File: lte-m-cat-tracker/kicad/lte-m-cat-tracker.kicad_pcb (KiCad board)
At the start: 2 copper layers, 30 x 35 mm, 32 parts, among them J1 JST-GH-1.25mm-2P, J2 USB-C-16P, SW1 MSK12C02, U1 SIM7080G-M, U2 ESP32-C3, U3 LIS2DW12TR, U4 TP4056, U5 XC6220B331MR-G

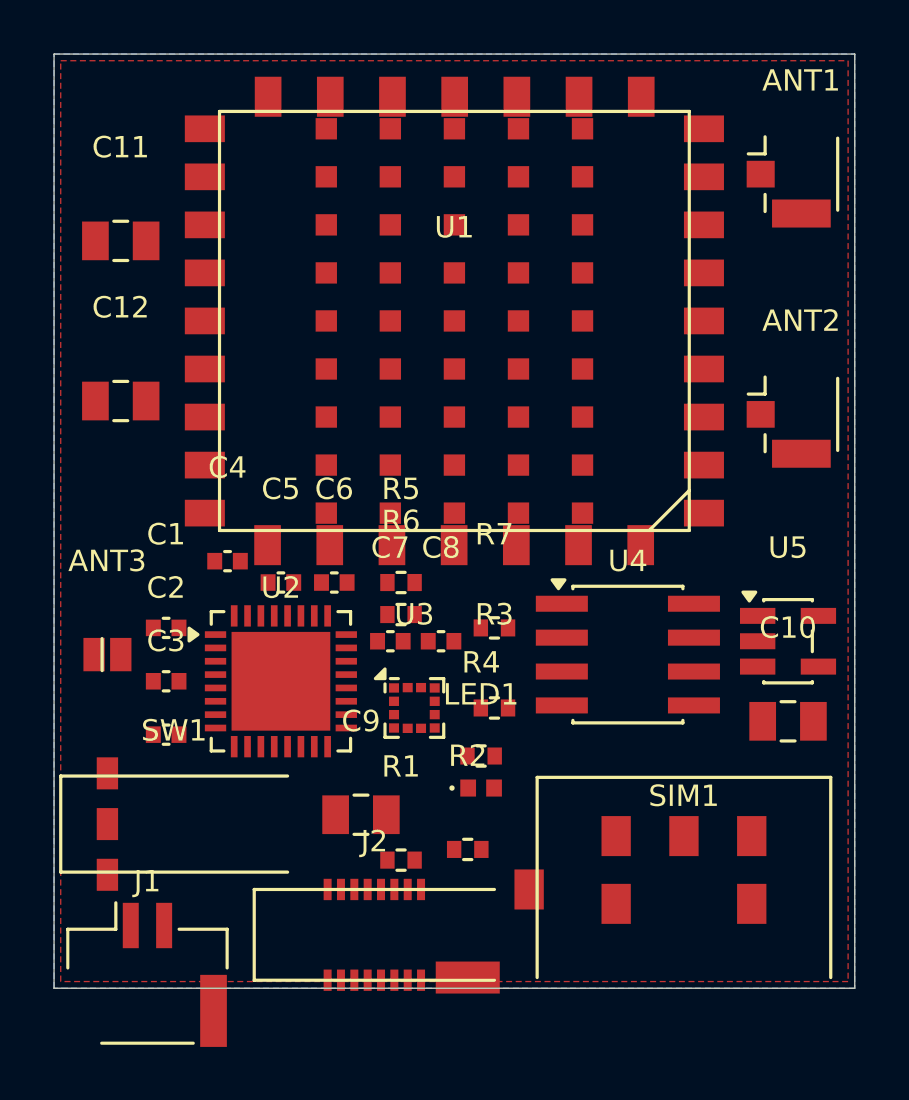
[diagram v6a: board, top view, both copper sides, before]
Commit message: route_pcb_v9.py: 短絡5件→0件達成（2026-06-07）
修正内容:
1. VBAT y=28.5迂回: LED1.pad1[GND](15.515,27.5)がVBATバスを短絡
2. +3.3V F.Cu y=20.5ジョグ: C5.pad2[GND]をF.Cu迂回（B.Cu y=19.0はSIM_TXDと交差）
3. SIM_RESETN y=24.5迂回: SIM_STATUS via(5.35,24.0)との接触を解消
4. U1 nonetパッド回避: via(10.02,19.0)削除→F.Cuスタブ直接接続
5. I2C_SCL y=25.2ジョグ: R3.pad1[nonet](15.99,24.5)を回避

DRC結果: 短絡0件 / 未配線11件（-2件）

Co-Authored-By: Claude Sonnet 4.6 <noreply@anthropic.com>
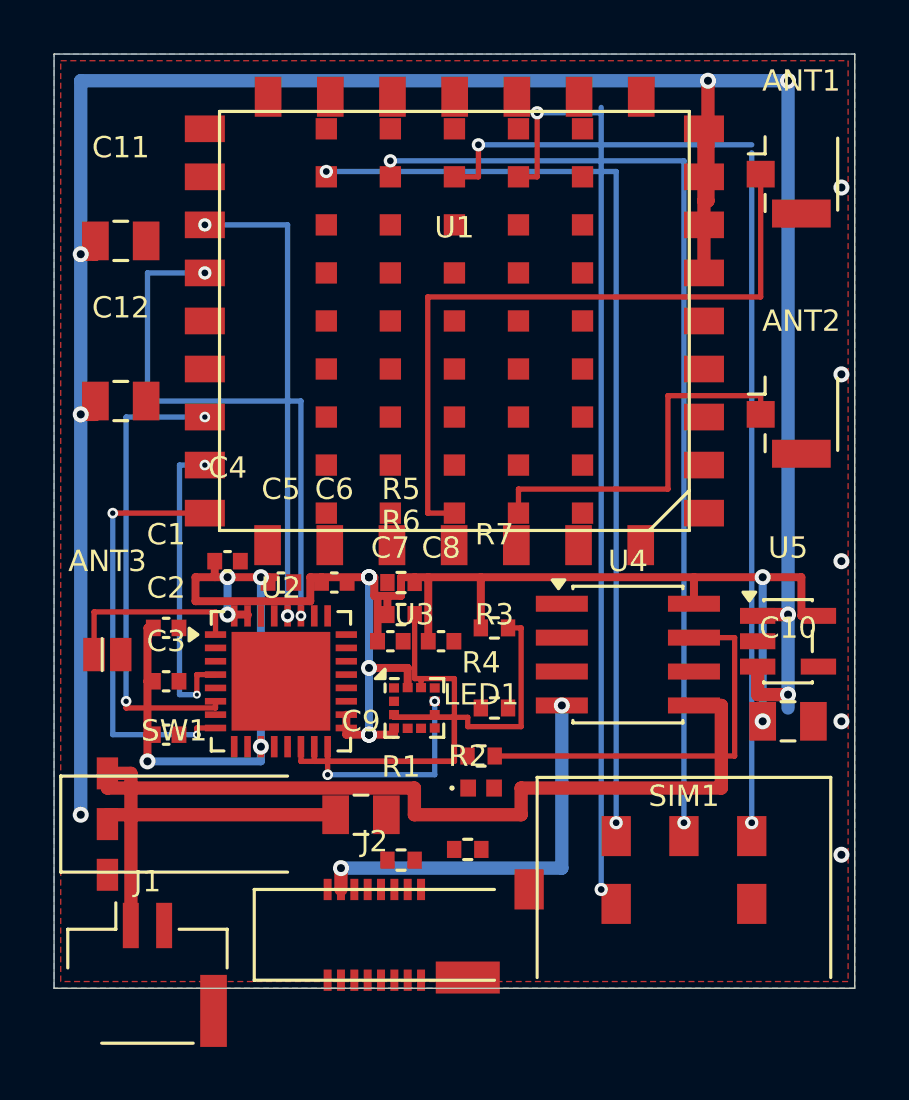
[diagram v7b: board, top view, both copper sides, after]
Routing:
- net VBAT_SW: track 0.00 -> 101.9 mm, vias 0 -> 7
- net +3.3V: track 0.00 -> 81.4 mm, vias 0 -> 12
- net SIM_CLK: track 0.00 -> 37.9 mm, vias 0 -> 2
- net SIM_DATA: track 0.00 -> 36.9 mm, vias 0 -> 2
- net VBAT: track 0.00 -> 36.2 mm
- net SIM_VDD: track 0.00 -> 36.0 mm, vias 0 -> 2
- net SIM_RST: track 0.00 -> 35.9 mm, vias 0 -> 2
- net LTE_ANT: track 0.00 -> 26.2 mm
- net SIM_TXD: track 0.00 -> 20.8 mm, vias 0 -> 2
- net I2C_SCL: track 0.00 -> 19.1 mm
- net SIM_RXD: track 0.00 -> 17.8 mm, vias 0 -> 2
- net SIM_RESETN: track 0.00 -> 17.5 mm, vias 0 -> 2
- net SIM_PWRKEY: track 0.00 -> 15.8 mm, vias 0 -> 2
- net VUSB: track 0.00 -> 15.2 mm, vias 0 -> 2
- net CHRG: track 0.00 -> 14.9 mm
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
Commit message: STEP3: C13配置追加・短絡0件達成（2026-06-07）
- add_c13.py: C13(100μF 6.3V polymer, 1210)をPCBに追加
  - 配置: (9.0, 33.3) J1右側・J2.A4 VUSBから十分離す
  - VBATタップ: y=31.0経由でJ1.pad2 GNDを回避
- route_pcb_v9.py: +3.3Vバス修正
  - seg(12.0,19.6→9.6,19.6)をC6.pad2 GNDとの短絡回避のためy=20.5ジョグに変更

DRC結果: 短絡0件 ✅ / 未配線43件（GNDゾーン未充填分）

Co-Authored-By: Claude Sonnet 4.6 <noreply@anthropic.com>
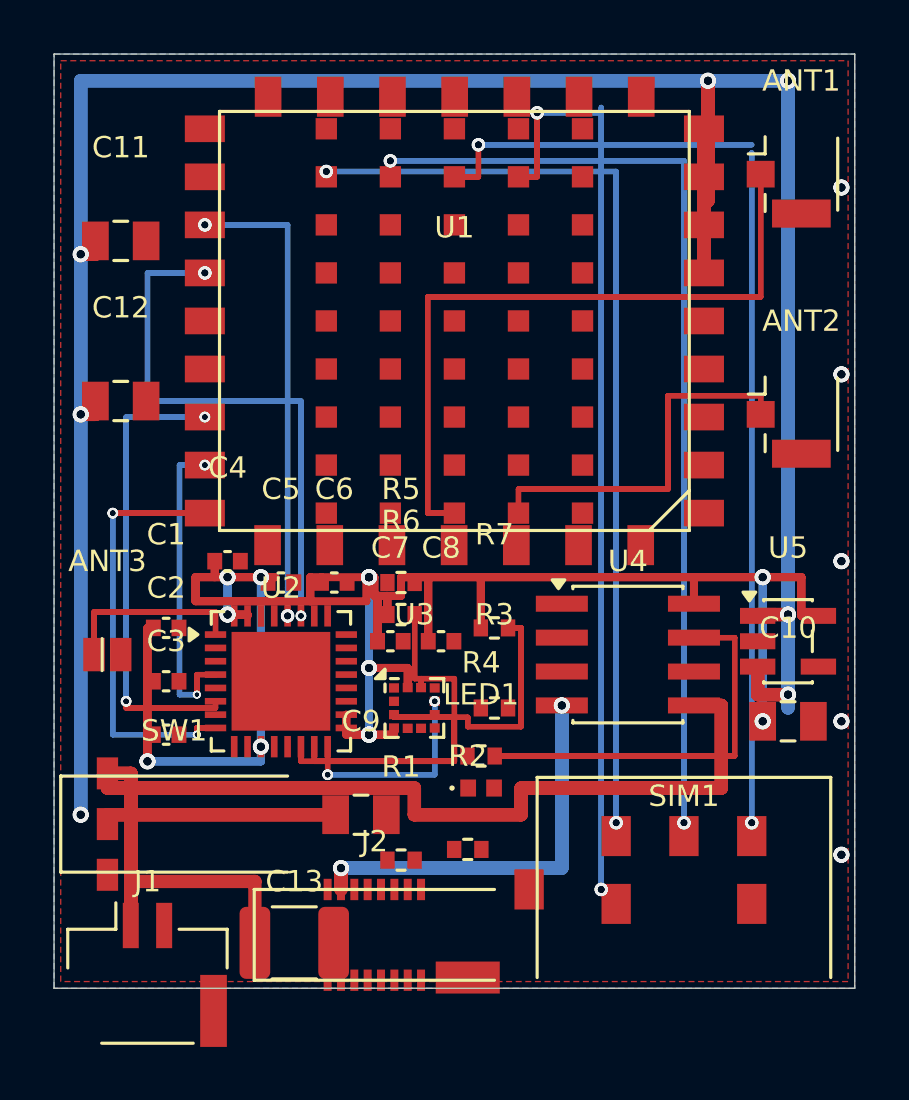
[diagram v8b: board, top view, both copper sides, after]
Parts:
- added C13: 100uF_6.3V_PolymerAl, Capacitor_SMD:C_1210_3225Metric, F.Cu at (9.00, 33.3)
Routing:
- net VBAT_SW: track 101.9 -> 203.8 mm, vias 7 -> 14
- net +3.3V: track 81.4 -> 163.6 mm, vias 12 -> 24
- net VBAT: track 36.2 -> 79.5 mm
- net SIM_CLK: track 37.9 -> 75.9 mm, vias 2 -> 4
- net SIM_DATA: track 36.9 -> 73.8 mm, vias 2 -> 4
- net SIM_VDD: track 36.0 -> 71.9 mm, vias 2 -> 4
- net SIM_RST: track 35.9 -> 71.8 mm, vias 2 -> 4
- net LTE_ANT: track 26.2 -> 52.4 mm
- net SIM_TXD: track 20.8 -> 41.5 mm, vias 2 -> 4
- net I2C_SCL: track 19.1 -> 38.2 mm
- net SIM_RXD: track 17.8 -> 35.5 mm, vias 2 -> 4
- net SIM_RESETN: track 17.5 -> 34.9 mm, vias 2 -> 4
- net SIM_PWRKEY: track 15.8 -> 31.7 mm, vias 2 -> 4
- net VUSB: track 15.2 -> 30.3 mm, vias 2 -> 4
- net CHRG: track 14.9 -> 29.9 mm
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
